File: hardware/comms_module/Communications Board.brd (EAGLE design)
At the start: 50 x 29 mm, 22 parts, among them U2 STC3115

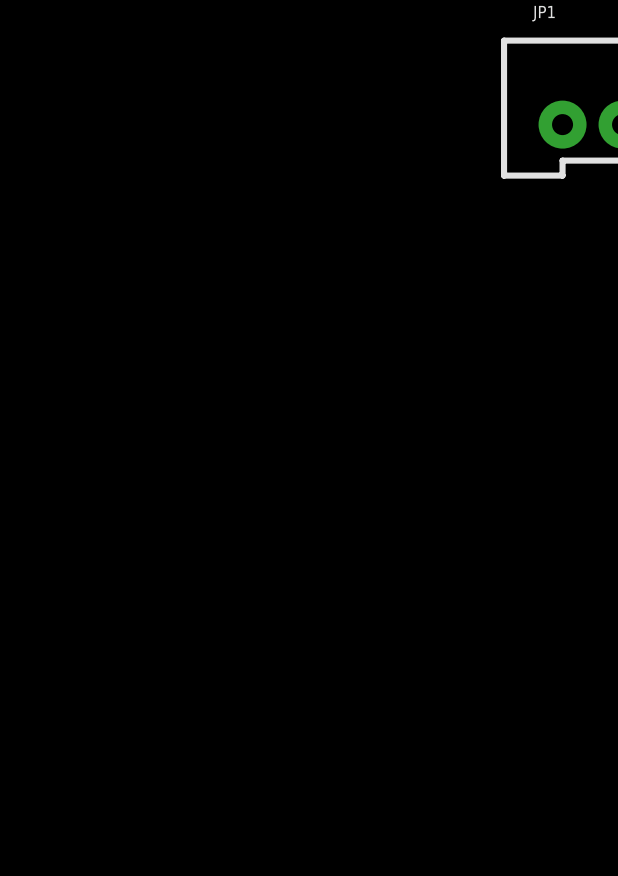
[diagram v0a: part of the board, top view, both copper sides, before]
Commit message: Add MUXes and moisture detection schematics.
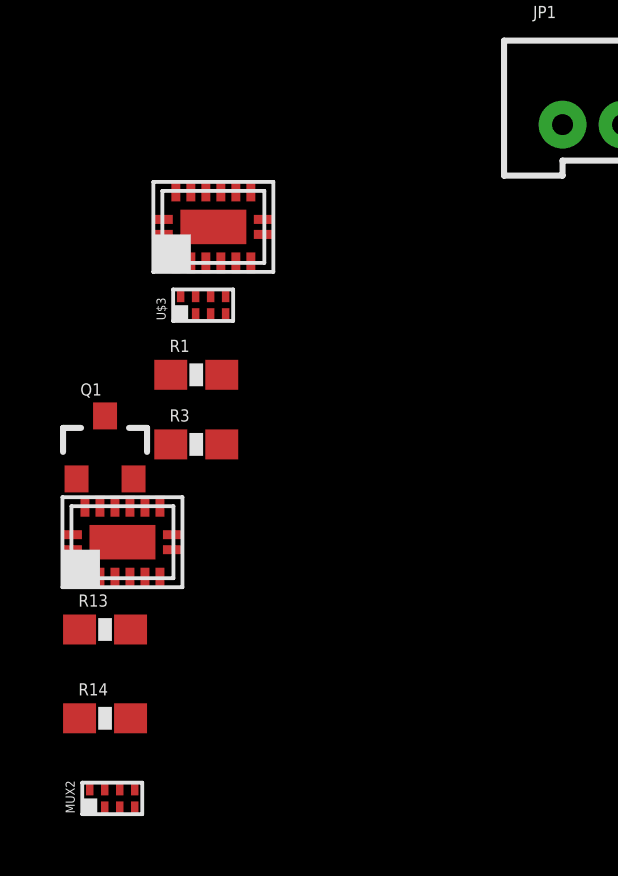
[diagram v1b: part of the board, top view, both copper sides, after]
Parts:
- added MCU: SABLE-X-BLE-MODULE, Capstone Library:SABLE-X-BLE-MODULE
- added MUX1: 74LV4051, Capstone Library:SOT763-1
- added MUX2, U$3: 74LVC2G53, Capstone Library:SOT833-1
- added Q1: MOSFET-PCHANNEL, SparkFun-DiscreteSemi:SOT23-3
- added R1, R13, R14, R3: 4K32_0.1%, SparkFun-Passives:0603-RES
- U$1: value SABLE-X-BLE-MODULE -> 74LV4051; device Capstone Library:SABLE-X-BLE-MODULE -> Capstone Library:SOT763-1
- moved U$1 32.9 mm to (-14.8, -12.7)
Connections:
- new net +1V3: MCU.30, R14.1, R3.1
- new net +3V3: MCU.11, MCU.12, Q1.3
- new net BANDAGE_A_0: MCU.29, MUX1.13, U$1.13
- new net BANDAGE_A_1: MUX1.14, U$1.14
- new net BANDAGE_A_2: MUX1.15, U$1.15
- new net BANDAGE_A_3: MUX1.12, U$1.12
- new net BANDAGE_A_4: MUX1.1, U$1.1
- new net BANDAGE_ID_0: U$1.5
- new net BANDAGE_ID_1: U$1.2
- new net CONN_STATE_RD: MCU.15, MUX1.3, MUX2.1, U$1.3, U$3.1
- new net DBG_LED: U$1.4
- new net JTAG_TCKC: MCU.7
- new net JTAG_TDI: MCU.14
- new net JTAG_TDO: MCU.13
- new net JTAG_TSMC: MCU.8
- new net MCU_RST: MCU.6
- new net MPSW: MCU.19, MUX2.5, U$3.5
- new net MP_EN_SW: MCU.24, MUX2.2, U$3.2
- new net MSW_0: MCU.23, MUX1.11, U$1.11
- new net MSW_1: MCU.21, MUX1.10, U$1.10
- new net MSW_2: MCU.20, MUX1.9, U$1.9
- new net N$11: U$1.7
- new net PERIPHERAL_PWR: MCU.18, Q1.1
- new net PERIPHERAL_VCC: MUX1.16, MUX1.PAD, MUX2.8, Q1.2, R1.1, R13.1, U$1.16, U$1.PAD, U$3.8
- new net VSENSE_0: MCU.32, MUX2.6, R1.2, R13.2, U$3.6
- new net VSENSE_1: MCU.31, MUX2.7, R14.2, R3.2, U$3.7
- net GND: now also MCU.2, MCU.22, MCU.3, MCU.33, MCU.34, MCU.35, MCU.36, MCU.37, MCU.38, MCU.39, MUX1.6, MUX1.7, MUX1.8, MUX2.3, MUX2.4, U$1.6, U$1.8, U$3.3, U$3.4
- net SCL: now also MCU.17
- net SDA: now also MCU.16

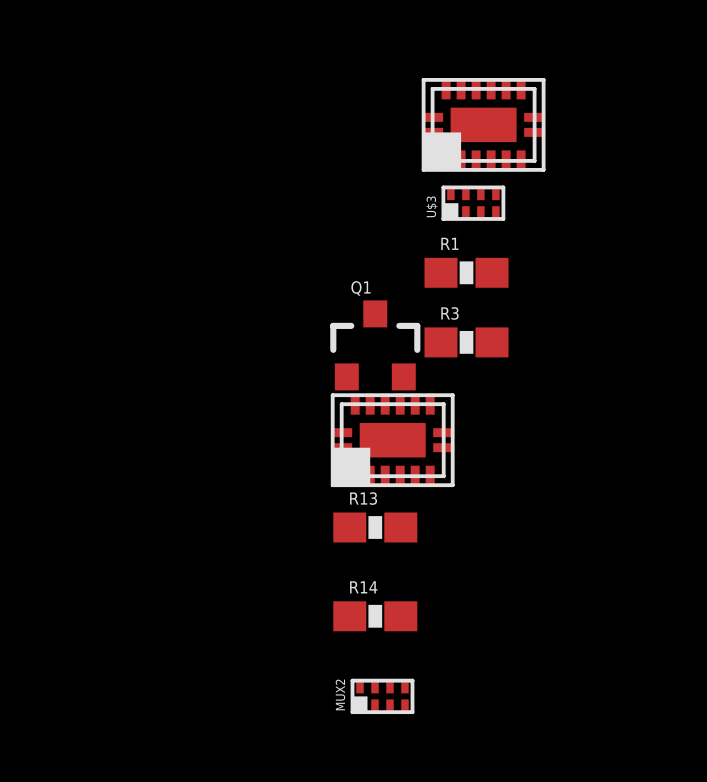
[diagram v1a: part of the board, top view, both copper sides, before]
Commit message: Add power management components.
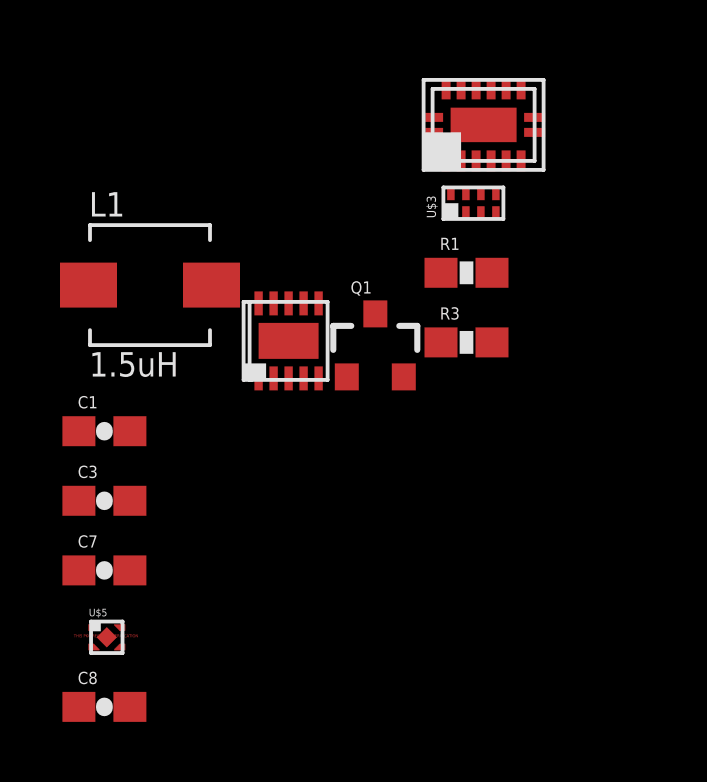
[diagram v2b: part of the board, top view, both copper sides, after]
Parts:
- removed MUX1: 74LV4051, Capstone Library:SOT763-1
- removed MUX2: 74LVC2G53, Capstone Library:SOT833-1
- removed R13, R14: 4K32_0.1%, SparkFun-Passives:0603-RES
- added C1, C3, C7, C8: (no value), SparkFun-Passives:0603-CAP
- added L1: 1.5uH, SparkFun-Passives:INDUCTOR-SRP4020
- added U$4: TPS63031, Capstone Library:SON-10
- added U$5: TLV717P, Capstone Library:X2SON
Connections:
- new net N$10: C3.1, U$4.6, U$4.7, U$4.8
- new net N$5: L1.P$1, U$4.4
- new net N$8: L1.P$2, U$4.2
- net +1V3: now also C8.1, U$5.1; no longer R14.1
- net +3V3: now also C7.1, U$4.1, U$4.10
- net BANDAGE_A_0: no longer MUX1.13
- net BANDAGE_A_1: no longer MUX1.14
- net BANDAGE_A_2: no longer MUX1.15
- net BANDAGE_A_3: no longer MUX1.12
- net BANDAGE_A_4: no longer MUX1.1
- net CONN_STATE_RD: no longer MUX1.3, MUX2.1
- net GND: now also C1.2, C3.2, C7.2, C8.2, U$4.3, U$4.9, U$4.PAD, U$5.2, U$5.PAD; no longer MUX1.6, MUX1.7, MUX1.8, MUX2.3, MUX2.4
- net MPSW: no longer MUX2.5
- net MP_EN_SW: no longer MUX2.2
- net MSW_0: no longer MUX1.11
- net MSW_1: no longer MUX1.10
- net MSW_2: no longer MUX1.9
- net PERIPHERAL_VCC: now also U$5.3, U$5.4; no longer MUX1.16, MUX1.PAD, MUX2.8, R13.1
- net VSENSE_0: no longer MUX2.6, R13.2
- net VSENSE_1: no longer MUX2.7, R14.2
- net V_PREBUCK: now also C1.1, U$4.5

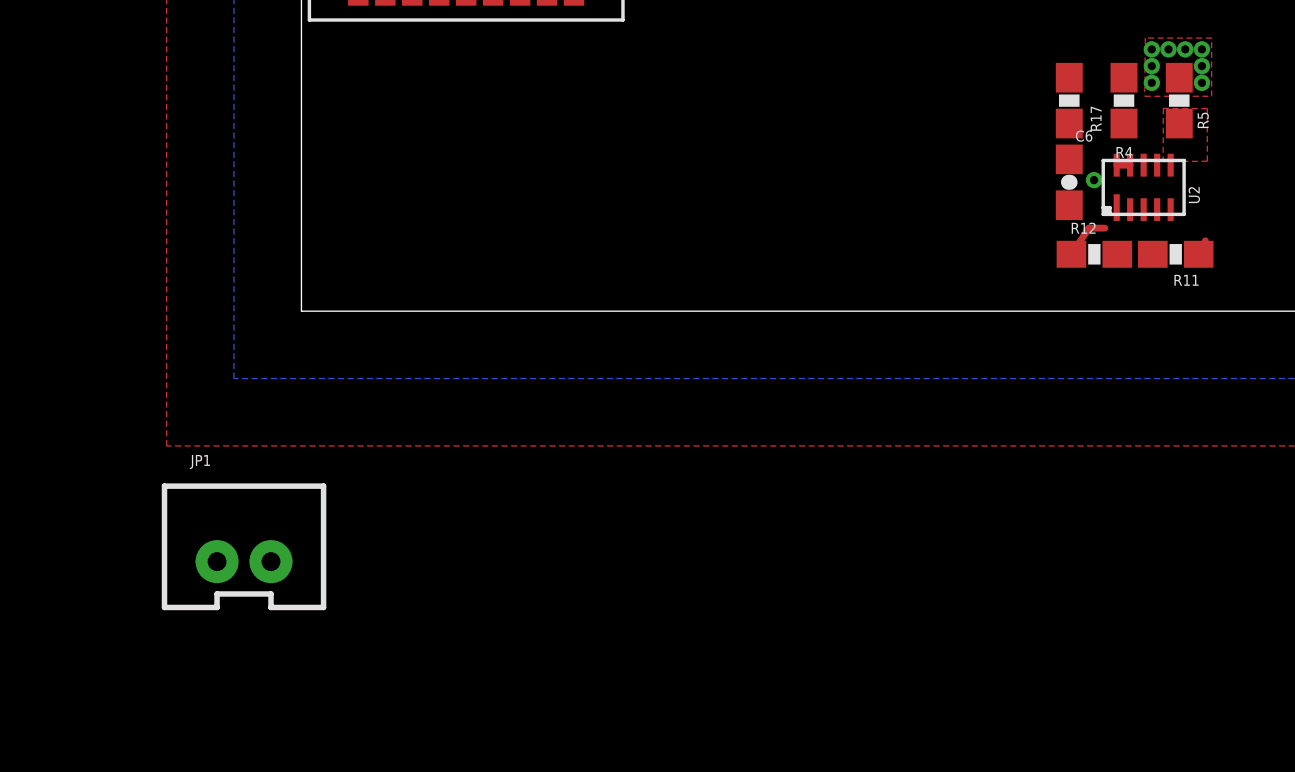
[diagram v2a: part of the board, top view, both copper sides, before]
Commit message: Fix STC3115 Vcc connection
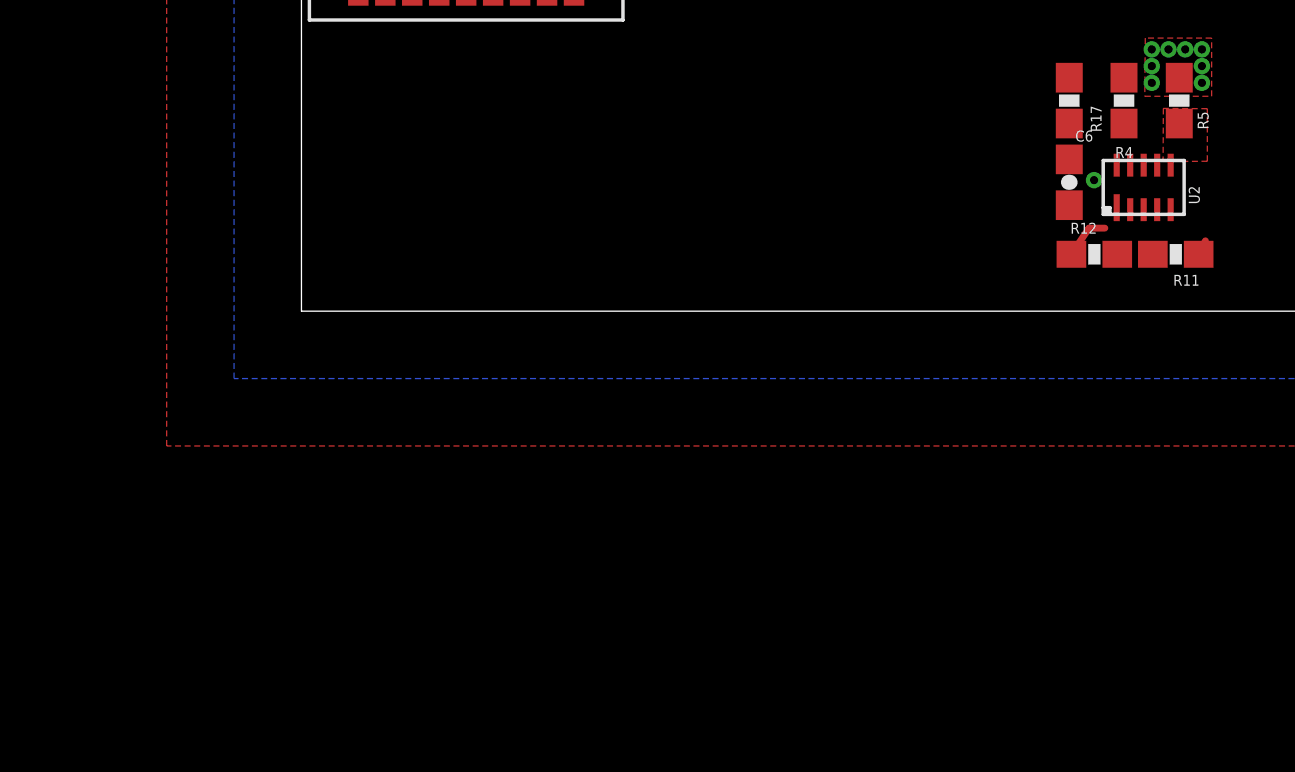
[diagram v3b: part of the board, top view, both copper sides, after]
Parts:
- removed JP1: (no value), SparkFun-Connectors:JST-2-PTH-VERT
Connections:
- net N$6: no longer U2.P9
- net VCC: now also U2.P9
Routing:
- net N$6: track 0.50 -> 0.00 mm
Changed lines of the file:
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@@
 <element name="SJ1" library="jumper" package="SJ" value="" x="23.25" y="15.82" rot="R270"/>
 <element name="MCU" library="Capstone Library" package="SABLE-X-BLE-MODULE" value="SABLE-X-BLE-MODULE" x="6.11" y="12.71"/>
-<element name="JP1" library="SparkFun-Connectors" package="JST-2-PTH-VERT" value="" x="-2.13" y="-8.74"/>
 <element name="TP1" library="testpad" package="TP16SQ" value="PTR1TP16SQ" x="29.42" y="20.07">
 <attribute name="TP_SIGNAL_NAME" value="" x="29.42" y="20.07" size="1.778" layer="27" display="off"/>
@@
 </signal>
 <signal name="N$6">
-<contactref element="U2" pad="P9"/>
 <contactref element="U2" pad="P10"/>
 <contactref element="C6" pad="1"/>
-<wire x1="30.74" y1="5.415" x2="30.24" y2="5.415" width="0.254" layer="1"/>
-<wire x1="30.24" y1="5.415" x2="28.48" y2="5.63" width="0" layer="19" extent="1-1"/>
+<wire x1="28.48" y1="5.63" x2="30.24" y2="5.415" width="0" layer="19" extent="1-1"/>
 </signal>
 <signal name="N$7">
@@
 <contactref element="R12" pad="2"/>
 <contactref element="R11" pad="2"/>
-<wire x1="30.26" y1="2.11" x2="31.58" y2="2.11" width="0" layer="19" extent="1-1"/>
+<contactref element="U2" pad="P9"/>
+<wire x1="30.26" y1="2.11" x2="30.74" y2="5.415" width="0" layer="19" extent="1-1"/>
+<wire x1="31.58" y1="2.11" x2="30.26" y2="2.11" width="0" layer="19" extent="1-1"/>
 </signal>
 <signal name="N$17">

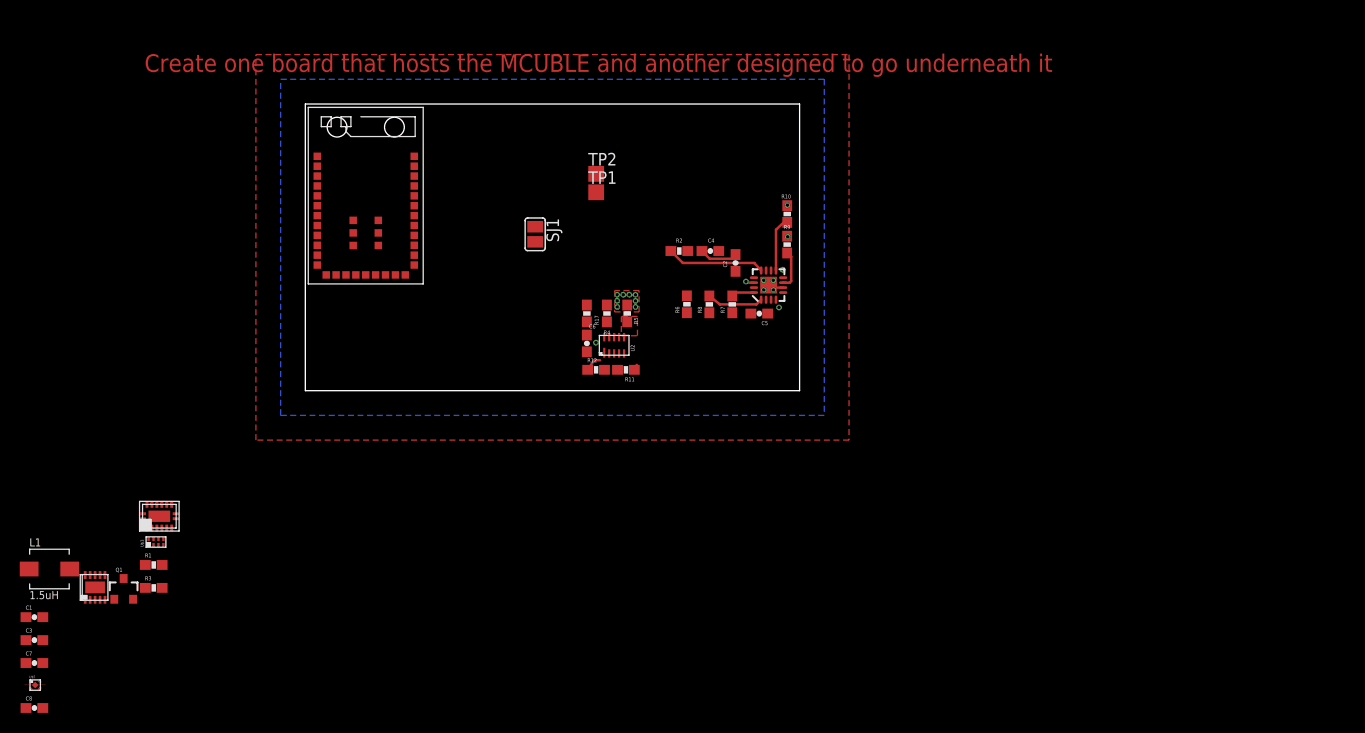
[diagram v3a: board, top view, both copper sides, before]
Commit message: Add remaining components and start board layout.
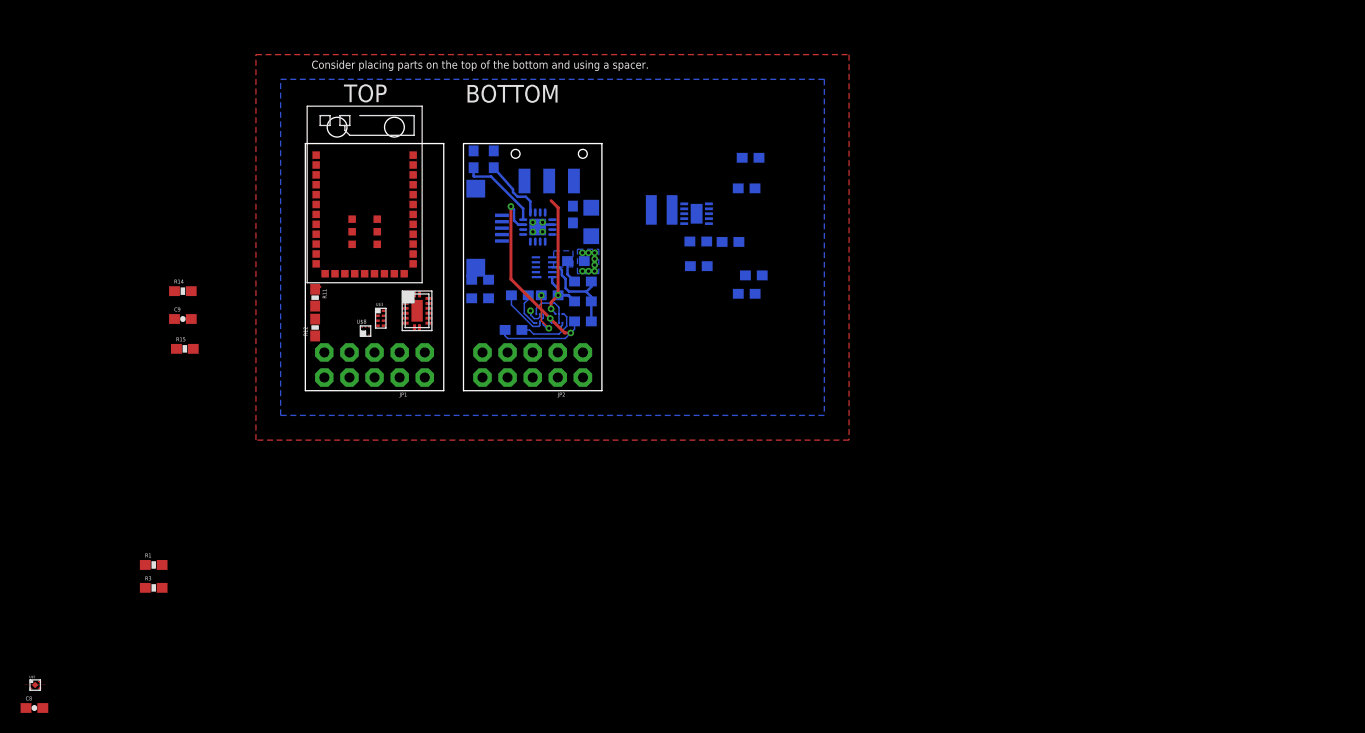
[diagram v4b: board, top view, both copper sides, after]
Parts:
- removed Q1: MOSFET-PCHANNEL, SparkFun-DiscreteSemi:SOT23-3
- removed R10, R9: 1k, SparkFun-Passives:0603-RES
- removed SJ1: (no value), jumper:SJ
- added C10: 10uF, SparkFun-Passives:0603-CAP
- added C9: 1uF, SparkFun-Passives:0603-CAP
- added JP1, JP2: (no value), SparkFun-Connectors:2X5_NOSILK
- added PSW: (no value), Capstone Library:JS102011SAQN
- added R13: 1Meg, SparkFun-Passives:0603-RES
- added R14, R16, R18: 100Meg, SparkFun-Passives:0603-RES
- added R15, R19: 10k, SparkFun-Passives:0603-RES
- added U$6, U$7, U$8: DMC2990UDJ, Capstone Library:SOT963
- added X2: USB-MICROB, SparkFun:USB-MICROB
- C1, C7: value (none) -> 10uF
- C3: value (none) -> 0.1uF
- L1: device SparkFun-Passives:INDUCTOR-SRP4020 -> Capstone Library:IND1212
- moved C7 82.7 mm to (45.4, 11.7), flipped to the bottom
- moved C3 81.1 mm to (43.0, 15.1), flipped to the bottom
- moved C1 76.0 mm to (39.8, 12.6), flipped to the bottom
- moved L1 71.8 mm to (36.0, 18.3), flipped to the bottom
- moved U$4 71.6 mm to (39.6, 17.9), flipped to the bottom, turned to 90 degrees
- moved U$1 33.3 mm to (11.3, 8.08), turned to 270 degrees
- moved R11 32.3 mm to (0.99, 9.41), turned to 270 degrees
- moved U$3 32.1 mm to (7.63, 7.33), turned to 270 degrees
- moved R7 30.0 mm to (17.0, 23.4), flipped to the bottom, turned to 270 degrees
- moved R12 28.7 mm to (0.99, 6.39), turned to 90 degrees
- moved R8 26.3 mm to (19.1, 23.4), flipped to the bottom, turned to 270 degrees
- moved C2 25.9 mm to (17.7, 11.2), flipped to the bottom, turned to 0 degrees
- moved U$2 24.1 mm to (23.5, 16.6), flipped to the bottom, turned to 270 degrees
- moved C5 21.3 mm to (27.1, 17.8), flipped to the bottom, turned to 270 degrees
- moved R2 20.7 mm to (17.7, 9.35), flipped to the bottom
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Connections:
- net BANDAGE_ID_0 renamed BANDAGE_DETECT
- removed net BANDAGE_ID_1: U$1.2
- removed net N$17: R9.1, U$2.7
- removed net N$18: R10.1, U$2.9
- removed net RSTIO: U2.P7
- new net /SYSDISBL: C9.1, R15.1, U$1.2
- new net AGND: JP1.5, JP2.5
- new net BATDC: R17.1, R4.2, R6.2, U2.P8
- new net N$12: R13.1, U$6.3
- new net N$13: JP1.8
- new net N$14: R14.1, R15.2, U$6.5
- new net N$15: JP1.6
- new net N$16: JP1.3
- new net N$21: R16.2, U$7.6
- new net N$22: R18.2, R19.2, U$6.4, U$7.2, U$7.5
- new net N$25: JP2.9
- new net N$26: JP2.8
- new net N$27: JP2.6
- new net N$28: JP2.3
- new net N$29: JP2.1
- new net N$9: R13.2, U$6.2, U$6.6
- new net SYSOFF: R16.1, R6.1, U$2.15, U$7.3
- net +3V3: now also C10.1, R19.1, U$8.4, U2.P9; no longer Q1.3
- net BAT+: now also C6.1, PSW.2, R17.2, R18.1, U$7.4, U2.P10; no longer TP2.TP
- net BAT-: now also C5.2
- net GND: now also C10.2, C9.2, JP1.7, JP2.7, R14.2, U$6.1, U$7.1, X2.GND; no longer C5.2, R6.1
- net JACK_PWR: now also X2.VBUS; no longer R17.2, SJ1.1
- net MCU_RST: now also U2.P7
- net N$19: now also JP1.1; no longer R6.2, SJ1.2, U$2.15
- net N$6: now also PSW.3, TP2.TP; no longer C6.1, U2.P10
- net N$7: now also JP1.9; no longer R17.1, R4.2, U2.P8
- net PERIPHERAL_PWR: now also U$8.5; no longer Q1.1
- net PERIPHERAL_VCC: now also JP1.10, JP2.10, U$8.3; no longer Q1.2
- net SCL: now also JP1.2, JP2.2
- net SDA: now also JP1.4, JP2.4
- net VCC: no longer U2.P9
- net V_PREBUCK: no longer R10.2, R9.2
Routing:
- net SYSOFF: track 0.00 -> 28.1 mm, vias 0 -> 3
- net BAT+: track 0.00 -> 16.2 mm, vias 0 -> 2
- net N$23: track 9.97 -> 0.00 mm
- net BATDC: track 0.00 -> 9.79 mm
- net N$21: track 0.00 -> 6.53 mm
- net N$9: track 0.00 -> 6.08 mm
- net N$24: track 2.33 -> 8.34 mm
- net N$18: track 5.90 -> 0.00 mm
- net N$22: track 0.00 -> 4.84 mm
- net N$17: track 4.15 -> 0.00 mm
- net N$12: track 0.00 -> 3.63 mm
- net BAT-: track 0.00 -> 2.35 mm
- net N$14: track 0.00 -> 2.01 mm, vias 0 -> 1
- net SDA: track 1.76 -> 0.00 mm
- net GND: track 5.38 -> 6.38 mm
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- added copper zone on layer 16, net BAT-
- removed copper zone on layer 1, net BAT-
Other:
- board size 50 x 29 mm -> 30 x 25 mm
- board text added: "BOTTOM"
- board text added: "Consider placing parts on the top of the bottom and using a spacer."
- board text added: "TOP"
- board text removed: "Create one board that hosts the MCUBLE and another designed to go underneath it"
